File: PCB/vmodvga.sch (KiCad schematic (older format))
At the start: 0 parts

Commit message: components added in schema
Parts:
- added J?: VHDCI, ~, symbol VHDCI
- added U?: AD9984, ~, symbol AD9984
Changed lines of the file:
@@
 LIBS:valves
 LIBS:vmodvga
+LIBS:vmodvga-cache
 EELAYER 27 0
 EELAYER END
@@
 Sheet 1 1
 Title ""
-Date ""
+Date "21 jul 2013"
 Rev ""
 Comp ""
@@
 Comment4 ""
 $EndDescr
+$Comp
+L AD9984 U?
+U 1 1 51EC3162
+P 6400 4000
+F 0 "U?" H 6500 3950 60  0000 C CNN
+F 1 "AD9984" H 6600 4050 60  0000 C CNN
+F 2 "~" H 5600 4250 60  0000 C CNN
+F 3 "~" H 5600 4250 60  0000 C CNN
+	1    6400 4000
+	1    0    0    -1
+$EndComp
+$Comp
+L VHDCI J?
+U 1 1 51EC3171
+P 10000 4000
+F 0 "J?" H 9650 2250 60  0000 C CNN
+F 1 "VHDCI" H 9750 5850 60  0000 C CNN
+F 2 "~" H 9600 5700 60  0000 C CNN
+F 3 "~" H 9600 5700 60  0000 C CNN
+	1    10000 4000
+	1    0    0    -1
+$EndComp
 $EndSCHEMATC

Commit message: CONN_15 Added
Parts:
- added J?: CONN_15, symbol CONN_15
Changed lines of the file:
@@
 	1    0    0    -1
 $EndComp
+$Comp
+L CONN_15 J?
+U 1 1 51EC34E7
+P 1050 4000
+F 0 "J?" V 1020 4000 60  0000 C CNN
+F 1 "CONN_15" V 1130 4000 60  0000 C CNN
+F 2 "" H 1050 4000 60  0000 C CNN
+F 3 "" H 1050 4000 60  0000 C CNN
+	1    1050 4000
+	-1   0    0    1
+$EndComp
 $EndSCHEMATC

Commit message: voltage regulator added
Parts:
- added C? (x12): .1uf, ~, symbol C
- added C?: 47uf, ~, symbol CP1
- added C? (x4): 22uf, ~, symbol CP1
- added C?: 4.7uf, ~, symbol CP1
- added FB? (x3): FILTER, ~, symbol FILTER
- added R? (x2): 76.8k, ~, symbol R
- added R? (x2): 147k, ~, symbol R
- added R? (x3): R, ~, symbol R
- added U?: ADP3303-3V3, ~, symbol ADP3303-3V3
- added U? (x2): ADP3334, ~, symbol ADP3334
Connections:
- net labels added: GND, HSYNC0, OVDD, PVD, VCC, VD, VSYNC0
- wire segments 0 -> 73
- no-connect marks 0 -> 4
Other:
- moved on the sheet: J?, U?

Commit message: Schema complete
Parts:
- removed FB? (x3): FILTER, ~, symbol FILTER
- removed R? (x3): R, ~, symbol R
- removed U?: AD9984, ~, symbol AD9984
- added C10, C26: 1nf, ~, symbol C
- added C11, C24, C25, C27, C8, C9: 47nf, ~, symbol C
- added C13: 10uf, ~, symbol C
- added C28: 0.008uf, ~, symbol C
- added C29: 0.08uf, ~, symbol C
- added FB1, FB2, FB3, FB4, FB5, FB6: FILTER, ~, symbol FILTER
- added J3: CONN_15, symbol CONN_15
- added R1, R10, R11, R12, R2, R3: 75, ~, symbol R
- added R13: 1k, ~, symbol R
- added R14: 1.5K, ~, symbol R
- added R15, R16: 10K, ~, symbol R
- added R17, R18: 1K, ~, symbol R
- added R6, R7: 2.2K, ~, symbol R
- added U4: AD9984, ~, symbol AD9984
- gave numbers to parts that had none: 27
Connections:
- net labels added: B0, B1, B2, B3, B4, B5, B6, B7, B8, B9, CLAMP, COST, DATACK, G0, G1, G2, G3, G4, G5, G6, G7, G8, G9, HSOUT, HSYNC1, OE_Field, PWRDWN, R0, R1, R2, R3, R4, R5, R6, R7, R8, R9, SCL, SDA, SOGOUT, VSOUT, VSYNC1
- wire segments 73 -> 284
- no-connect marks 4 -> 18
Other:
- moved on the sheet: C1, C12, C15, C17, C18, C4, C6, J2, R4, R5, U1

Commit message: LST and BOM generated
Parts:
- C15: renamed from C28; value 0.008uf -> 8.2nf
- C16: renamed from C29; value 0.08uf -> 82nf
- J1: renamed from J3; value CONN_15 -> DE-15
- J2: renamed from J1; value CONN_15 -> DE-15
- R7: renamed from R13; value 1k -> 1K
- renumbered C3 to C1, C25 to C10, C26 to C11, C11 to C12, C27 to C13, C13 to C14, C20 to C17, C21 to C18, C22 to C19, C5 to C2, C23 to C20, C4 to C21, C6 to C22, C12 to C23, C15 to C24, C17 to C25, C18 to C26, C7 to C3, C14 to C4, C16 to C5, C8 to C6, C24 to C7, C9 to C8, C10 to C9, C2 to Cp1, C19 to Cp2, C1 to Cp3, J2 to J3, R16 to R10, R17 to R11, R18 to R12, R8 to R13, R9 to R14, R6 to R15, R7 to R16, R4 to R17, R5 to R18, R10 to R4, R11 to R5, R12 to R6, R14 to R8, R15 to R9, U2 to U1, U3 to U2, U4 to U3, U1 to U4

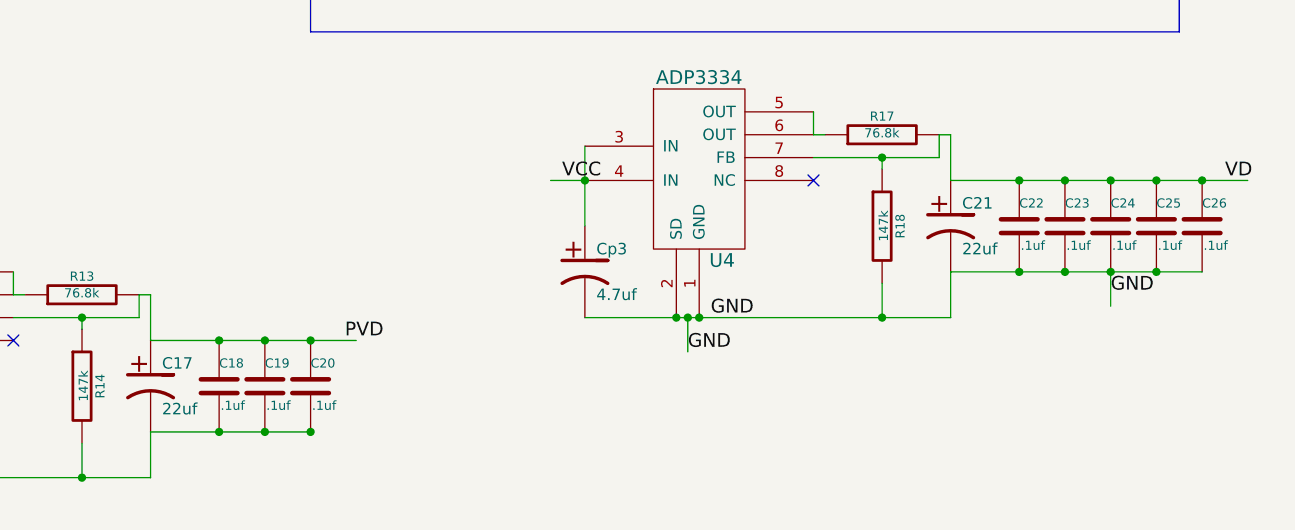
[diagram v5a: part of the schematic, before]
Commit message: Corrected one wrong label and footprint
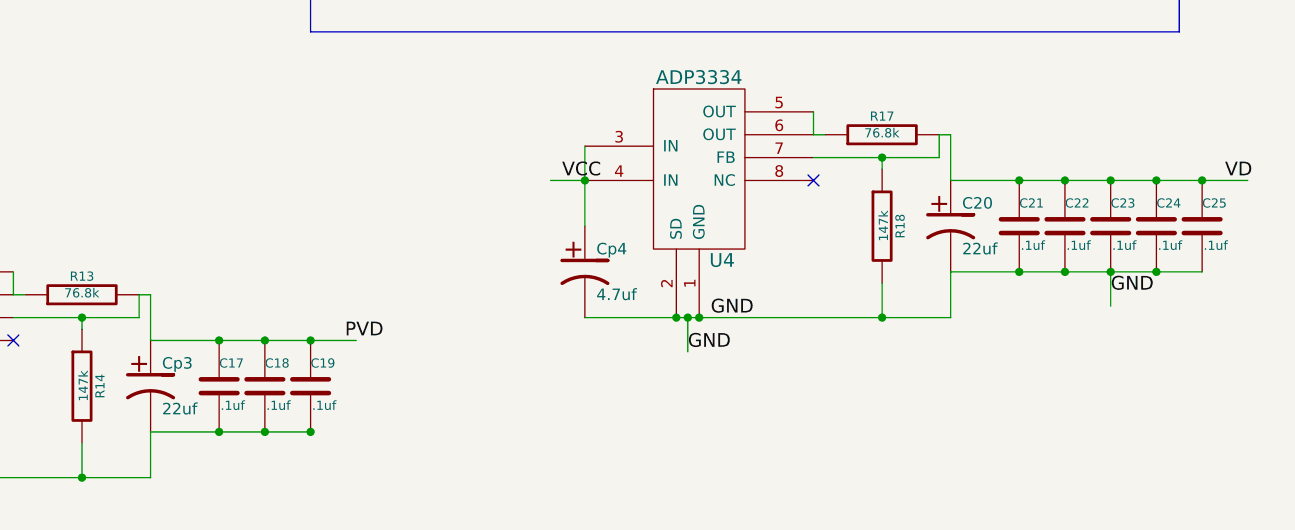
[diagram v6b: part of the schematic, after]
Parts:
- renumbered C18 to C17, C19 to C18, C20 to C19, C21 to C20, C22 to C21, C23 to C22, C24 to C23, C25 to C24, C26 to C25, C17 to Cp3, Cp3 to Cp4
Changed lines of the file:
@@
 $EndComp
 $Comp
-L CP1 Cp3
+L CP1 Cp4
 U 1 1 51EC3E79
 P 7900 6650
-F 0 "Cp3" H 7950 6750 50  0000 L CNN
+F 0 "Cp4" H 7950 6750 50  0000 L CNN
 F 1 "4.7uf" H 7950 6550 50  0000 L CNN
 F 2 "~" H 7900 6650 60  0000 C CNN
@@
 $EndComp
 $Comp
-L CP1 C21
+L CP1 C20
 U 1 1 51EC40C9
 P 9500 6450
-F 0 "C21" H 9550 6550 50  0000 L CNN
+F 0 "C20" H 9550 6550 50  0000 L CNN
 F 1 "22uf" H 9550 6350 50  0000 L CNN
 F 2 "~" H 9500 6450 60  0000 C CNN
@@
 $EndComp
 $Comp
-L C C22
+L C C21
 U 1 1 51EC4164
 P 9800 6450
-F 0 "C22" H 9800 6550 40  0000 L CNN
+F 0 "C21" H 9800 6550 40  0000 L CNN
 F 1 ".1uf" H 9806 6365 40  0000 L CNN
 F 2 "~" H 9838 6300 30  0000 C CNN
@@
 $EndComp
 $Comp
-L C C23
+L C C22
 U 1 1 51EC417D
 P 10000 6450
-F 0 "C23" H 10000 6550 40  0000 L CNN
+F 0 "C22" H 10000 6550 40  0000 L CNN
 F 1 ".1uf" H 10006 6365 40  0000 L CNN
 F 2 "~" H 10038 6300 30  0000 C CNN
@@
 $EndComp
 $Comp
-L C C24
+L C C23
 U 1 1 51EC4183
 P 10200 6450
-F 0 "C24" H 10200 6550 40  0000 L CNN
+F 0 "C23" H 10200 6550 40  0000 L CNN
 F 1 ".1uf" H 10206 6365 40  0000 L CNN
 F 2 "~" H 10238 6300 30  0000 C CNN
@@
 $EndComp
 $Comp
-L C C25
+L C C24
 U 1 1 51EC4189
 P 10400 6450
-F 0 "C25" H 10400 6550 40  0000 L CNN
+F 0 "C24" H 10400 6550 40  0000 L CNN
 F 1 ".1uf" H 10406 6365 40  0000 L CNN
 F 2 "~" H 10438 6300 30  0000 C CNN
@@
 $EndComp
 $Comp
-L C C26
+L C C25
 U 1 1 51EC418F
 P 10600 6450
-F 0 "C26" H 10600 6550 40  0000 L CNN
+F 0 "C25" H 10600 6550 40  0000 L CNN
 F 1 ".1uf" H 10606 6365 40  0000 L CNN
 F 2 "~" H 10638 6300 30  0000 C CNN
@@
 $EndComp
 $Comp
-L CP1 C17
+L CP1 Cp3
 U 1 1 51EC485A
 P 6000 7150
-F 0 "C17" H 6050 7250 50  0000 L CNN
+F 0 "Cp3" H 6050 7250 50  0000 L CNN
 F 1 "22uf" H 6050 7050 50  0000 L CNN
 F 2 "~" H 6000 7150 60  0000 C CNN
@@
 $EndComp
 $Comp
-L C C18
+L C C17
 U 1 1 51EC4860
 P 6300 7150
-F 0 "C18" H 6300 7250 40  0000 L CNN
+F 0 "C17" H 6300 7250 40  0000 L CNN
 F 1 ".1uf" H 6306 7065 40  0000 L CNN
 F 2 "~" H 6338 7000 30  0000 C CNN
@@
 $EndComp
 $Comp
-L C C19
+L C C18
 U 1 1 51EC4866
 P 6500 7150
-F 0 "C19" H 6500 7250 40  0000 L CNN
+F 0 "C18" H 6500 7250 40  0000 L CNN
 F 1 ".1uf" H 6506 7065 40  0000 L CNN
 F 2 "~" H 6538 7000 30  0000 C CNN
@@
 $EndComp
 $Comp
-L C C20
+L C C19
 U 1 1 51EC486C
 P 6700 7150
-F 0 "C20" H 6700 7250 40  0000 L CNN
+F 0 "C19" H 6700 7250 40  0000 L CNN
 F 1 ".1uf" H 6706 7065 40  0000 L CNN
 F 2 "~" H 6738 7000 30  0000 C CNN

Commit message: Initial component placement
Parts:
- renumbered C1 to Cp5, C20 to Cp6
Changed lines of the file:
@@
 NoConn ~ 1950 6550
 $Comp
-L CP1 C1
+L CP1 Cp5
 U 1 1 51EC3BC1
 P 2200 6900
-F 0 "C1" H 2250 7000 50  0000 L CNN
+F 0 "Cp5" H 2250 7000 50  0000 L CNN
 F 1 "22uf" H 2250 6800 50  0000 L CNN
 F 2 "~" H 2200 6900 60  0000 C CNN
@@
 $EndComp
 $Comp
-L CP1 C20
+L CP1 Cp6
 U 1 1 51EC40C9
 P 9500 6450
-F 0 "C20" H 9550 6550 50  0000 L CNN
+F 0 "Cp6" H 9550 6550 50  0000 L CNN
 F 1 "22uf" H 9550 6350 50  0000 L CNN
 F 2 "~" H 9500 6450 60  0000 C CNN

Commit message: Started with PCB design
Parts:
- added P1, P2, P3, P4: 50R, symbol DIL16
- added R19, R20, R21, R22: 50, ~, symbol R
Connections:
- wire segments 284 -> 228
- no-connect marks 18 -> 20
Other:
- moved on the sheet: J3
